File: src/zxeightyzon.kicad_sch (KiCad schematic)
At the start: 21 parts, among them J1 01x10, U1 YM2149, U2 GAL16V8

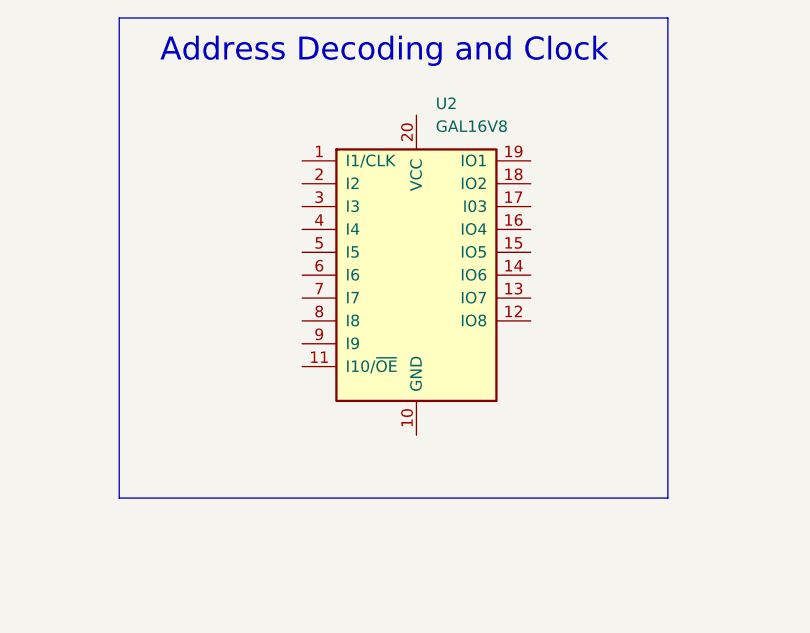
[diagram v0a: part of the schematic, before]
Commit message: change schematic to 22v10 and added outline base for pCB
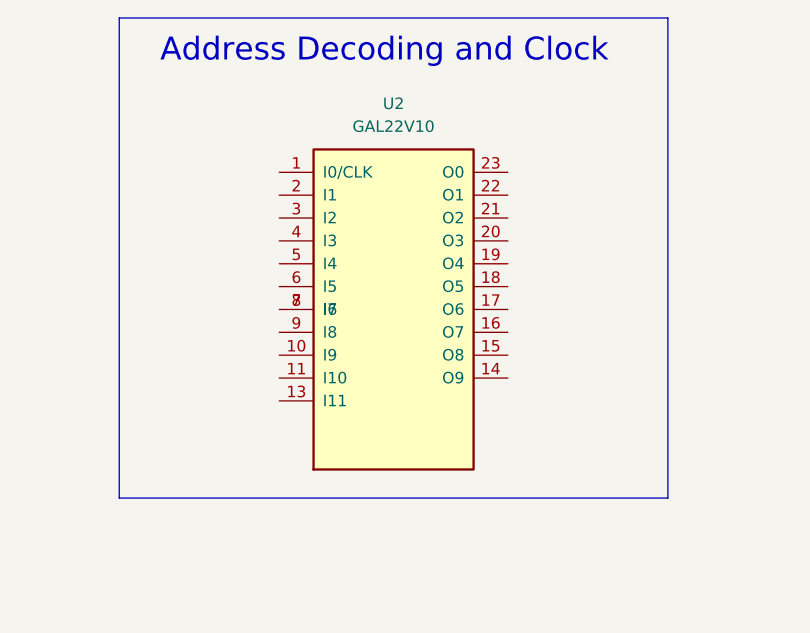
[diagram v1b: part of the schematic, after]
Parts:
- removed U2: GAL16V8, symbol Logic_Programmable:GAL16V8
- added U2: GAL22V10, symbol GAL22V10:GAL22V10
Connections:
- net GND: now also U2.12 (GND)
- net VCC: now also U2.24 (VCC)
- new net: U2.7 (I6), U2.8 (I7)
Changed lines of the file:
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@@
-	)
-	(symbol
-		(lib_id "Logic_Programmable:GAL16V8")
-		(at 182.88 44.45 0)
-		(unit 1)
-		(exclude_from_sim no)
-		(in_bom yes)
-		(on_board yes)
-		(dnp no)
-		(fields_autoplaced yes)
-		(property "Reference" "U2"
-			(at 185.0233 25.4 0)
-			(effects
-				(font
-					(size 1.27 1.27)
-				)
-				(justify left)
-			)
-		)
-		(property "Value" "GAL16V8"
-			(at 185.0233 27.94 0)
-			(effects
-				(font
-					(size 1.27 1.27)
-				)
-				(justify left)
-			)
-		)
-		(property "Footprint" ""
-			(at 182.88 44.45 0)
-			(effects
-				(font
-					(size 1.27 1.27)
-				)
-				(hide yes)
-			)
-		)
-		(property "Datasheet" ""
-			(at 182.88 44.45 0)
-			(effects
-				(font
-					(size 1.27 1.27)
-				)
-				(hide yes)
-			)
-		)
-		(property "Description" "Programmable Logic Array, DIP-20/SOIC-20/PLCC-20"
-			(at 182.88 44.45 0)
-			(effects
-				(font
-					(size 1.27 1.27)
-				)
-				(hide yes)
-			)
-		)
-		(pin "20"
-		)
-		(pin "18"
-		)
-		(pin "6"
-		)
-		(pin "1"
-		)
-		(pin "2"
-		)
-		(pin "5"
-		)
-		(pin "17"
-		)
-		(pin "10"
-		)
-		(pin "11"
-		)
-		(pin "14"
-		)
-		(pin "4"
-		)
-		(pin "7"
-		)
-		(pin "8"
-		)
-		(pin "3"
-		)
-		(pin "9"
-		)
-		(pin "19"
-		)
-		(pin "16"
-		)
-		(pin "13"
-		)
-		(pin "12"
-		)
-		(pin "15"
-		)
-		(instances
-			(project ""
-				(path "/826cb6a0-960b-4c84-b856-fb110427ba7d"
-					(reference "U2")
-					(unit 1)
-				)
-			)
-		)
 	)
 	(symbol
@@
 					(unit 1)
 				)
+			)
+		)
+	)
+	(symbol
+		(lib_id "GAL22V10:GAL22V10")
+		(at 180.34 48.26 0)
+		(unit 1)
+		(exclude_from_sim no)
+		(in_bom yes)
+		(on_board yes)
+		(dnp no)
+		(fields_autoplaced yes)
+		(property "Reference" "U2"
+			(at 180.34 25.4 0)
+			(effects
+				(font
+					(size 1.27 1.27)
+				)
+			)
+		)
+		(property "Value" "GAL22V10"
+			(at 180.34 27.94 0)
+			(effects
+				(font
+					(size 1.27 1.27)
+				)
+			)
+		)
+		(property "Footprint" ""
+			(at 180.34 48.26 0)
+			(effects
+				(font
+					(size 1.27 1.27)
+				)
+				(hide yes)
+			)
+		)
+		(property "Datasheet" ""
+			(at 180.34 48.26 0)
+			(effects
+				(font
+					(size 1.27 1.27)
+				)
+				(hide yes)
+			)
+		)
+		(property "Description" ""
+			(at 180.34 48.26 0)
+			(effects
+				(font
+					(size 1.27 1.27)
+				)
+				(hide yes)
+			)
+		)
+		(pin "1"
+		)
+		(pin "22"
+		)
+		(pin "3"
+		)
+		(pin "5"
+		)
+		(pin "14"
+		)
+		(pin "10"
+		)
+		(pin "21"
+		)
+		(pin "8"
+		)
+		(pin "11"
+		)
+		(pin "16"
+		)
+		(pin "13"
+		)
+		(pin "12"
+		)
+		(pin "23"
+		)
+		(pin "4"
+		)
+		(pin "6"
+		)
+		(pin "7"
+		)
+		(pin "20"
+		)
+		(pin "18"
+		)
+		(pin "17"
+		)
+		(pin "19"
+		)
+		(pin "15"
+		)
+		(pin "2"
+		)
+		(pin "9"
+		)
+		(pin "24"
+		)
+		(instances
+			(project ""
+				(path "/826cb6a0-960b-4c84-b856-fb110427ba7d"
+					(reference "U2")
+					(unit 1)
+				)

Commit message: started schematic
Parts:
- added J2, J3: 01x10, Connector_PinHeader_2.54mm:PinHeader_1x10_P2.54mm_Vertical, symbol Connector:Conn_01x10_Pin
- added JP2: CLK Select, symbol Jumper:Jumper_3_Open
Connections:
- net A0: now also U2.2 (I1)
- net A1: now also U2.3 (I2)
- net A2: now also U2.4 (I3)
- net A3: now also U2.5 (I4)
- net A4: now also U2.6 (I5)
- net A5: now also U2.8 (I7)
- net A6: now also U2.7 (I6)
- net A7: now also U2.9 (I8)
- net CH_A: now also U1.3 (A)
- net CH_B: now also U1.4 (B)
- net CH_C: now also U1.38 (C)
- net CLK: now also U2.1 (I0/CLK)
- net D0: now also U1.37 (DA0)
- net D1: now also U1.36 (DA1)
- net D2: now also U1.35 (DA2)
- net D3: now also U1.34 (DA3)
- net D4: now also U1.33 (DA4)
- net D5: now also U1.32 (DA5)
- net D6: now also U1.31 (DA6)
- net D7: now also U1.30 (DA7)
- net GND: now also U1.1 (VSS), U1.24 (~{A9}), J2.10 (Pin_10), J3.10 (Pin_10), J3.9 (Pin_9)
- net IOA0: now also U1.21 (IOA0)
- net IOA1: now also U1.20 (IOA1)
- net IOA2: now also U1.19 (IOA2)
- net IOA3: now also U1.18 (IOA3)
- net IOA4: now also U1.17 (IOA4)
- net IOA5: now also U1.16 (IOA5)
- net IOA6: now also U1.15 (IOA6)
- net IOA7: now also U1.14 (IOA7)
- net VCC: now also U1.25 (A8), U1.28 (BC2), U1.40 (VCC), J2.1 (Pin_1), J3.1 (Pin_1), J3.2 (Pin_2)
- net ~{IOREQ}: now also U2.11 (I10)
- net ~{RD}: now also U2.13 (I11)
- net ~{RESET}: now also U1.23 (~{RESET})
- net ~{WR}: now also U2.10 (I9)
- net IOB3: now reaches U1.10 (IOB3)
- net IOB3: now also J2.5 (Pin_5)
- net IOB2: now reaches U1.11 (IOB2)
- net IOB2: now also J2.4 (Pin_4)
- net IOB1: now reaches U1.12 (IOB1)
- net IOB1: now also J2.3 (Pin_3)
- net IOB0: now reaches U1.13 (IOB0)
- net IOB0: now also J2.2 (Pin_2)
- net at U1.22 (CLOCK): now also JP2.2 (C)
- net BDIR: now reaches U1.27 (BDIR)
- net BDIR: now also U2.14 (O9)
- net BC1: now reaches U1.29 (BC1)
- net BC1: now also U2.15 (O8)
- net IOB7: now reaches U1.6 (IOB7)
- net IOB7: now also J2.9 (Pin_9)
- net IOB6: now reaches U1.7 (IOB6)
- net IOB6: now also J2.8 (Pin_8)
- net IOB5: now reaches U1.8 (IOB5)
- net IOB5: now also J2.7 (Pin_7)
- net IOB4: now reaches U1.9 (IOB4)
- net IOB4: now also J2.6 (Pin_6)
- net CLK_DIV2: now reaches U2.16 (O7)
- net CLK_DIV2: now also JP2.3 (B)
- net CLK_OUT: now reaches U2.17 (O6)
- net CLK_OUT: now also JP2.1 (A)
- net O5: now reaches U2.18 (O5)
- net O5: now also J3.8 (Pin_8)
- net O4: now reaches U2.19 (O4)
- net O4: now also J3.7 (Pin_7)
- net O3: now reaches U2.20 (O3)
- net O3: now also J3.6 (Pin_6)
- net O2: now reaches U2.21 (O2)
- net O2: now also J3.5 (Pin_5)
- net O1: now reaches U2.22 (O1)
- net O1: now also J3.4 (Pin_4)
- net O0: now reaches U2.23 (O0)
- net O0: now also J3.3 (Pin_3)
- no-connect marks 22 -> 23
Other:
- moved on the sheet: C1, C2, C3, C4, C5, C6, CO1, CO2, FB1, J1, JP1, R2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

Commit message: started PCB layout
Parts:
- added J4: Conn_02x02_Top_Bottom, Connector_PinHeader_2.54mm:PinHeader_2x02_P2.54mm_Vertical, symbol Connector_Generic:Conn_02x02_Top_Bottom
- JP2: footprint (none) -> Connector_PinHeader_2.54mm:PinHeader_1x03_P2.54mm_Vertical
- U1: footprint Package_DIP:DIP-40_W15.24mm_Socket_LongPads -> Package_DIP:DIP-40_W15.24mm_LongPads
- U2: footprint (none) -> Package_DIP:DIP-24_W7.62mm_LongPads
- renumbered C2 to C1, C1 to C2
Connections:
- net CH_A renamed A_OUT
- net CH_B: no longer names the net of R4.2, R5.2
- net CH_B: now also J4.3 (Pin_3); no longer U1.4 (B)
- net CH_C: no longer names the net of R3.1
- net CH_C: now also J4.2 (Pin_2); no longer U1.38 (C)
- new net B_OUT: J4.1 (Pin_1), U1.4 (B)
- new net C_OUT: J4.4 (Pin_4), U1.38 (C)
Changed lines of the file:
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@@
 	(wire
 		(pts
+			(xy 151.13 119.38) (xy 151.13 125.73)
+		)
+		(stroke
+			(width 0)
+			(type default)
+		)
+	)
+	(wire
+		(pts
 			(xy 210.82 109.22) (xy 203.2 109.22)
 		)
@@
 	(wire
 		(pts
+			(xy 160.02 119.38) (xy 153.67 119.38)
+		)
+		(stroke
+			(width 0)
+			(type default)
+		)
+	)
+	(wire
+		(pts
 			(xy 245.11 133.35) (xy 254 133.35)
 		)
@@
 	(wire
 		(pts
+			(xy 182.88 111.76) (xy 182.88 125.73)
+		)
+		(stroke
+			(width 0)
+			(type default)
+		)
+	)
+	(wire
+		(pts
 			(xy 78.74 40.64) (xy 73.66 40.64)
 		)
@@
 	(wire
 		(pts
+			(xy 140.97 106.68) (xy 151.13 106.68)
+		)
+		(stroke
+			(width 0)
+			(type default)
+		)
+	)
+	(wire
+		(pts
 			(xy 250.19 71.12) (xy 250.19 63.5)
 		)
@@
 	(wire
 		(pts
+			(xy 173.99 119.38) (xy 195.58 119.38)
+		)
+		(stroke
+			(width 0)
+			(type default)
+		)
+	)
+	(wire
+		(pts
 			(xy 72.39 93.98) (xy 67.31 93.98)
 		)
@@
 	(wire
 		(pts
+			(xy 153.67 106.68) (xy 173.99 106.68)
+		)
+		(stroke
+			(width 0)
+			(type default)
+		)
+	)
+	(wire
+		(pts
 			(xy 257.81 48.26) (xy 257.81 40.64)
 		)
@@
 	(wire
 		(pts
-			(xy 182.88 119.38) (xy 195.58 119.38)
+			(xy 181.61 64.77) (xy 177.8 64.77)
 		)
 		(stroke
@@
 	(wire
 		(pts
-			(xy 181.61 64.77) (xy 177.8 64.77)
+			(xy 29.21 40.64) (xy 34.29 40.64)
 		)
 		(stroke
@@
 	(wire
 		(pts
-			(xy 29.21 40.64) (xy 34.29 40.64)
+			(xy 173.99 106.68) (xy 173.99 119.38)
 		)
 		(stroke
@@
 	(wire
 		(pts
+			(xy 151.13 125.73) (xy 182.88 125.73)
+		)
+		(stroke
+			(width 0)
+			(type default)
+		)
+	)
+	(wire
+		(pts
 			(xy 236.22 48.26) (xy 236.22 40.64)
 		)
@@
 		)
 	)
-	(label "CH_B"
-		(at 182.88 111.76 180)
-		(effects
-			(font
-				(size 1.27 1.27)
-			)
-			(justify right bottom)
-		)
-	)
 	(label "IOA0"
 		(at 215.9 48.26 90)
@@
 		)
 	)
-	(label "CH_A"
+	(label "A_OUT"
 		(at 100.33 123.19 0)
 		(effects
@@
 		)
 	)
-	(label "CH_A"
+	(label "A_OUT"
 		(at 182.88 104.14 180)
 		(effects
@@
 		)
 	)
+	(label "B_OUT"
+		(at 140.97 106.68 0)
+		(effects
+			(font
+				(size 1.27 1.27)
+			)
+			(justify left bottom)
+		)
+	)
 	(label "O0"
 		(at 237.49 71.12 90)
@@
 		)
 	)
-	(label "CH_C"
+	(label "C_OUT"
 		(at 100.33 128.27 0)
 		(effects
@@
 		)
 	)
-	(label "CH_B"
+	(label "B_OUT"
 		(at 100.33 125.73 0)
 		(effects
@@
 		)
 	)
+	(label "C_OUT"
+		(at 160.02 119.38 0)
+		(effects
+			(font
+				(size 1.27 1.27)
+			)
+			(justify left bottom)
+		)
+	)
 	(label "A3"
 		(at 147.32 52.07 180)
@@
 		)
 	)
-	(label "CH_C"
-		(at 182.88 119.38 180)
-		(effects
-			(font
-				(size 1.27 1.27)
-			)
-			(justify right bottom)
-		)
-	)
 	(symbol
 		(lib_id "Jumper:Jumper_2_Bridged")
@@
 			)
 		)
-		(property "Footprint" "Package_DIP:DIP-40_W15.24mm_Socket_LongPads"
+		(property "Footprint" "Package_DIP:DIP-40_W15.24mm_LongPads"
 			(at 99.06 184.15 0)
 			(effects
@@
 		(on_board yes)
 		(dnp no)
-		(property "Reference" "C2"
+		(property "Reference" "C1"
 			(at 223.52 101.854 90)
 			(effects
@@
 			(project "zxeightyzon"
 				(path "/826cb6a0-960b-4c84-b856-fb110427ba7d"
-					(reference "C2")
+					(reference "C1")
 					(unit 1)
 				)
@@
 	)
 	(symbol
+		(lib_id "Connector_Generic:Conn_02x02_Top_Bottom")
+		(at 151.13 111.76 90)
+		(mirror x)
+		(unit 1)
+		(exclude_from_sim no)
+		(in_bom yes)
+		(on_board yes)
+		(dnp no)
+		(property "Reference" "J4"
+			(at 149.352 113.03 90)
+			(effects
+				(font
+					(size 1.27 1.27)
+				)
+				(justify left)
+			)
+		)
+		(property "Value" "Conn_02x02_Top_Bottom"
+			(at 156.21 111.7601 90)
+			(effects
+				(font
+					(size 1.27 1.27)
+				)
+				(justify right)
+				(hide yes)
+			)
+		)
+		(property "Footprint" "Connector_PinHeader_2.54mm:PinHeader_2x02_P2.54mm_Vertical"
+			(at 151.13 111.76 0)
+			(effects
+				(font
+					(size 1.27 1.27)
+				)
+				(hide yes)
+			)
+		)
+		(property "Datasheet" "~"
+			(at 151.13 111.76 0)
+			(effects
+				(font
+					(size 1.27 1.27)
+				)
+				(hide yes)
+			)
+		)
+		(property "Description" "Generic connector, double row, 02x02, top/bottom pin numbering scheme (row 1: 1...pins_per_row, row2: pins_per_row+1 ... num_pins), script generated (kicad-library-utils/schlib/autogen/connector/)"
+			(at 151.13 111.76 0)
+			(effects
+				(font
+					(size 1.27 1.27)
+				)
+				(hide yes)
+			)
+		)
+		(pin "1"
+		)
+		(pin "2"
+		)
+		(pin "3"
+		)
+		(pin "4"
+		)
+		(instances
+			(project ""
+				(path "/826cb6a0-960b-4c84-b856-fb110427ba7d"
+					(reference "J4")
+					(unit 1)
+				)
+			)
+		)
+	)
+	(symbol
 		(lib_id "Connector:Conn_01x10_Pin")
 		(at 223.52 35.56 90)
@@
 			)
 		)
-		(property "Footprint" ""
+		(property "Footprint" "Package_DIP:DIP-24_W7.62mm_LongPads"
 			(at 165.1 55.88 0)
 			(effects
@@
 		(on_board yes)
 		(dnp no)
-		(property "Reference" "C1"
+		(property "Reference" "C2"
 			(at 223.52 117.094 90)
 			(effects
@@
 			(project "zxeightyzon"
 				(path "/826cb6a0-960b-4c84-b856-fb110427ba7d"
-					(reference "C1")
+					(reference "C2")
 					(unit 1)
 				)
@@
 			)
 		)
-		(property "Footprint" ""
+		(property "Footprint" "Connector_PinHeader_2.54mm:PinHeader_1x03_P2.54mm_Vertical"
 			(at 35.56 158.75 0)
 			(effects
